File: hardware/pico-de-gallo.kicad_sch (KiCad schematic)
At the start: 7 parts, among them J1 Conn_01x04_Socket, J2 Conn_01x05_Socket, J3 Conn_01x08_Pin

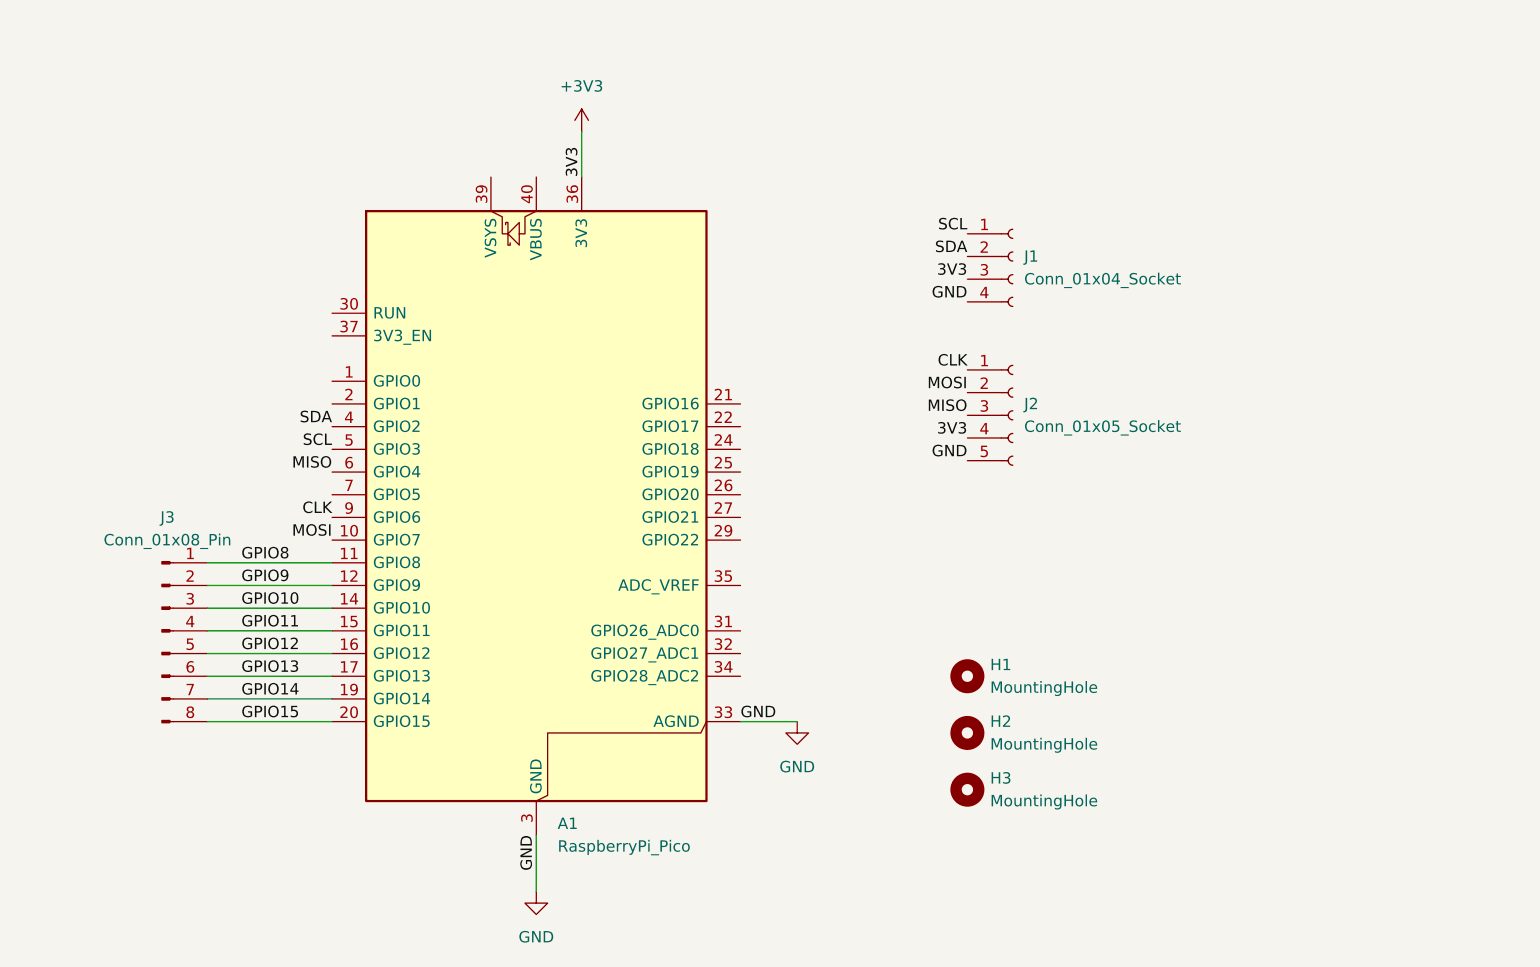
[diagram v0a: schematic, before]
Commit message: hardware: fix DRC and ERC
Signed-off-by: Felipe Balbi <febalbi@microsoft.com>
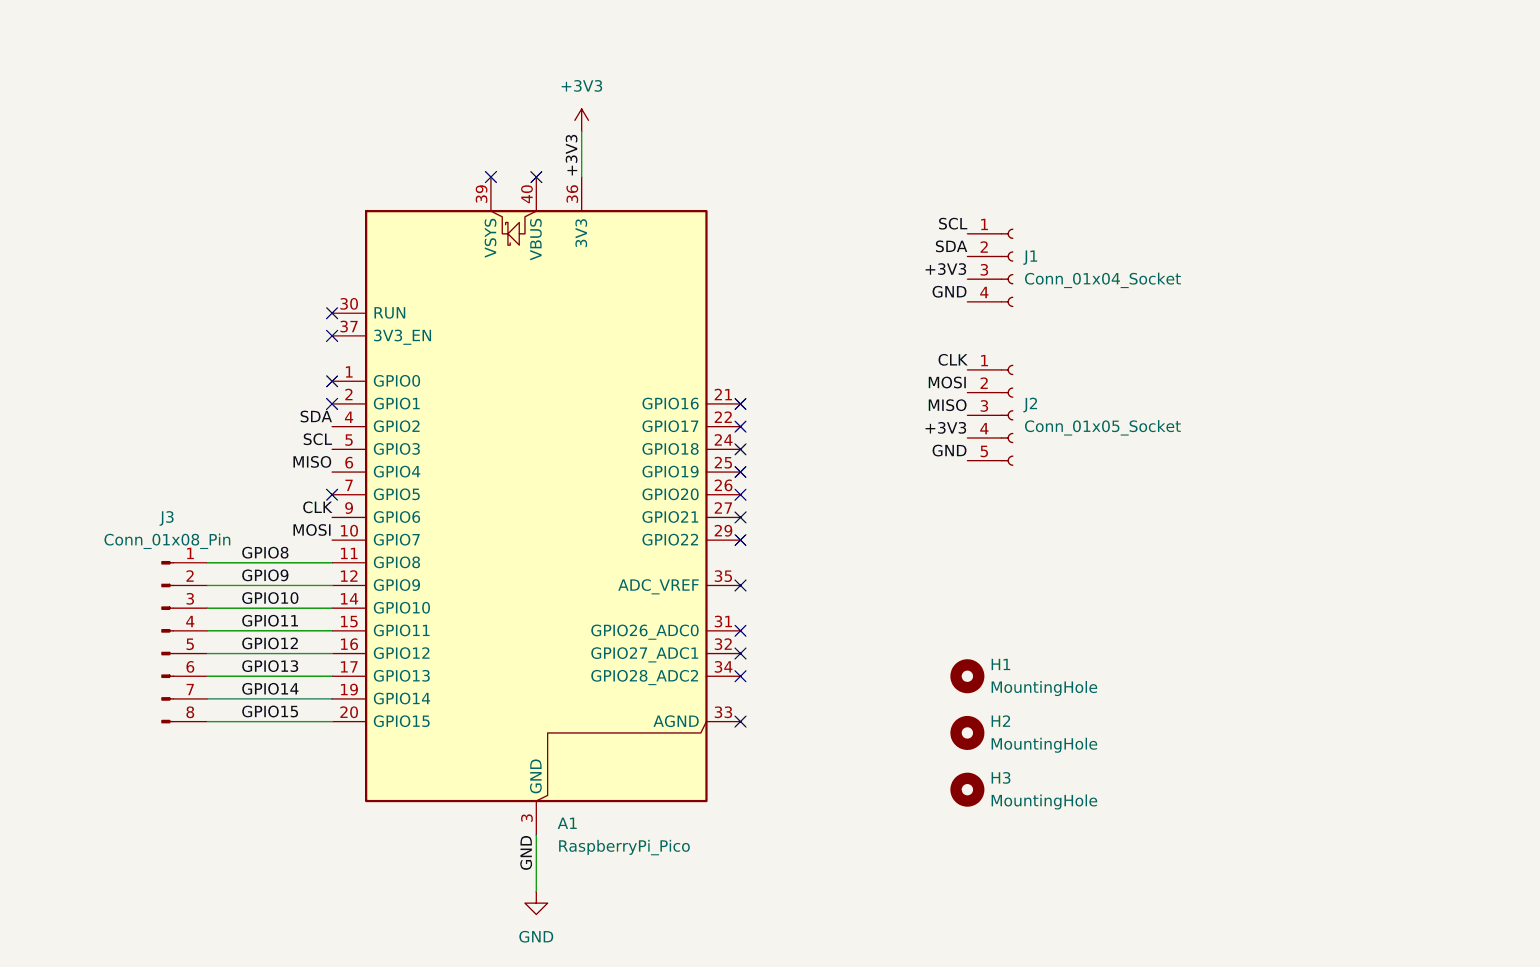
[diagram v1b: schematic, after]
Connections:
- net GND: no longer A1.33 (AGND)
- no-connect marks 0 -> 19
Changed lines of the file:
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@@
 	(generator_version "9.0")
 	(paper "A4")
+	(no_connect
+		(at 146.05 57.15)
+	)
+	(no_connect
+		(at 168.91 87.63)
+	)
+	(no_connect
+		(at 123.19 80.01)
+	)
+	(no_connect
+		(at 123.19 72.39)
+	)
+	(no_connect
+		(at 168.91 82.55)
+	)
+	(no_connect
+		(at 168.91 102.87)
+	)
+	(no_connect
+		(at 168.91 85.09)
+	)
+	(no_connect
+		(at 168.91 90.17)
+	)
+	(no_connect
+		(at 168.91 95.25)
+	)
+	(no_connect
+		(at 168.91 118.11)
+	)
+	(no_connect
+		(at 168.91 92.71)
+	)
+	(no_connect
+		(at 123.19 92.71)
+	)
+	(no_connect
+		(at 123.19 74.93)
+	)
+	(no_connect
+		(at 168.91 110.49)
+	)
+	(no_connect
+		(at 168.91 97.79)
+	)
+	(no_connect
+		(at 140.97 57.15)
+	)
+	(no_connect
+		(at 123.19 82.55)
+	)
+	(no_connect
+		(at 168.91 113.03)
+	)
+	(no_connect
+		(at 168.91 107.95)
+	)
 	(wire
 		(pts
@@
 		(pts
 			(xy 151.13 52.07) (xy 151.13 57.15)
-		)
-		(stroke
-			(width 0)
-			(type default)
-		)
-	)
-	(wire
-		(pts
-			(xy 168.91 118.11) (xy 175.26 118.11)
 		)
 		(stroke
@@
 		)
 	)
-	(label "3V3"
+	(label "+3V3"
 		(at 151.13 57.15 90)
 		(effects
@@
 		)
 	)
-	(label "3V3"
+	(label "+3V3"
 		(at 194.31 68.58 180)
 		(effects
@@
 	)
 	(label "GND"
-		(at 168.91 118.11 0)
-		(effects
-			(font
-				(size 1.27 1.27)
-			)
-			(justify left bottom)
-		)
-	)
-	(label "GND"
 		(at 194.31 88.9 180)
 		(effects
@@
 		)
 	)
-	(label "3V3"
+	(label "+3V3"
 		(at 194.31 86.36 180)
 		(effects
@@
 					(unit 1)
 				)
-			)
-		)
-	)
-	(symbol
-		(lib_id "power:GND")
-		(at 175.26 118.11 0)
-		(unit 1)
-		(exclude_from_sim no)
-		(in_bom yes)
-		(on_board yes)
-		(dnp no)
-		(fields_autoplaced yes)
-		(property "Reference" "#PWR02"
-			(at 175.26 124.46 0)
-			(effects
-				(font
-					(size 1.27 1.27)
-				)
-				(hide yes)
-			)
-		)
-		(property "Value" "GND"
-			(at 175.26 123.19 0)
-			(effects
-				(font
-					(size 1.27 1.27)
-				)
-			)
-		)
-		(property "Footprint" ""
-			(at 175.26 118.11 0)
-			(effects
-				(font
-					(size 1.27 1.27)
-				)
-				(hide yes)
-			)
-		)
-		(property "Datasheet" ""
-			(at 175.26 118.11 0)
-			(effects
-				(font
-					(size 1.27 1.27)
-				)
-				(hide yes)
-			)
-		)
-		(property "Description" "Power symbol creates a global label with name \"GND\" , ground"
-			(at 175.26 118.11 0)
-			(effects
-				(font
-					(size 1.27 1.27)
-				)
-				(hide yes)
-			)
-		)
-		(pin "1"
-		)
-		(instances
-			(project "pico-de-gallo"
-				(path "/409a2a34-92f9-4daa-b11b-cb64dd13f272"
-					(reference "#PWR02")
-					(unit 1)
-				)

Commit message: update case and PCB
Signed-off-by: Felipe Balbi <febalbi@microsoft.com>
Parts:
- removed J1: Conn_01x04_Socket, Connector_PinSocket_2.54mm:PinSocket_1x04_P2.54mm_Horizontal, symbol Connector:Conn_01x04_Socket
- removed J2: Conn_01x05_Socket, Connector_PinSocket_2.54mm:PinSocket_1x05_P2.54mm_Horizontal, symbol Connector:Conn_01x05_Socket
- removed J3: Conn_01x08_Pin, Connector_PinHeader_2.54mm:PinHeader_1x08_P2.54mm_Vertical, symbol Connector:Conn_01x08_Pin
- added J1: Conn_02x08_Odd_Even, Connector_PinHeader_2.54mm:PinHeader_2x08_P2.54mm_Vertical, symbol Connector_Generic:Conn_02x08_Odd_Even
- added J2, J5: Conn_01x02, Connector_PinHeader_2.54mm:PinHeader_1x02_P2.54mm_Vertical, symbol Connector_Generic:Conn_01x02
- added J3: Conn_01x04, Connector_PinHeader_2.54mm:PinHeader_1x04_P2.54mm_Vertical, symbol Connector_Generic:Conn_01x04
- added J4: Conn_01x05, Connector_PinHeader_2.54mm:PinHeader_1x05_P2.54mm_Vertical, symbol Connector_Generic:Conn_01x05
- added J6: Conn_01x03, Connector_PinHeader_2.54mm:PinHeader_1x03_P2.54mm_Vertical, symbol Connector_Generic:Conn_01x03
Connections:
- net +3V3: now also J2.1 (Pin_1), J3.3 (Pin_3), J4.4 (Pin_4)
- net CLK: now also J4.1 (Pin_1), J6.1 (Pin_1)
- net GND: now also J2.2 (Pin_2), J3.4 (Pin_4), J4.5 (Pin_5)
- net GPIO10: now also J1.5 (Pin_5), J1.6 (Pin_6)
- net GPIO11: now also J1.7 (Pin_7), J1.8 (Pin_8)
- net GPIO12: now also J1.10 (Pin_10), J1.9 (Pin_9)
- net GPIO13: now also J1.11 (Pin_11), J1.12 (Pin_12)
- net GPIO14: now also J1.13 (Pin_13), J1.14 (Pin_14)
- net GPIO15: now also J1.15 (Pin_15), J1.16 (Pin_16)
- net GPIO8: now also J1.1 (Pin_1), J1.2 (Pin_2)
- net GPIO9: now also J1.3 (Pin_3), J1.4 (Pin_4)
- net MISO: now also J4.3 (Pin_3), J6.3 (Pin_3)
- net MOSI: now also J4.2 (Pin_2), J6.2 (Pin_2)
- net SCL: now also J3.1 (Pin_1), J5.1 (Pin_1)
- net SDA: now also J3.2 (Pin_2), J5.2 (Pin_2)

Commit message: Update PCB
Signed-off-by: Felipe Balbi <febalbi@microsoft.com>
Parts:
- J3: footprint Connector_PinHeader_2.54mm:PinHeader_1x04_P2.54mm_Vertical -> Connector_PinSocket_2.54mm:PinSocket_1x04_P2.54mm_Horizontal
- J4: footprint Connector_PinHeader_2.54mm:PinHeader_1x05_P2.54mm_Vertical -> Connector_PinSocket_2.54mm:PinSocket_1x05_P2.54mm_Horizontal
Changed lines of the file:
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@@
 			)
 		)
-		(property "Footprint" "Connector_PinHeader_2.54mm:PinHeader_1x04_P2.54mm_Vertical"
+		(property "Footprint" "Connector_PinSocket_2.54mm:PinSocket_1x04_P2.54mm_Horizontal"
 			(at 199.39 66.04 0)
 			(effects
@@
 			)
 		)
-		(property "Footprint" "Connector_PinHeader_2.54mm:PinHeader_1x05_P2.54mm_Vertical"
+		(property "Footprint" "Connector_PinSocket_2.54mm:PinSocket_1x05_P2.54mm_Horizontal"
 			(at 199.39 83.82 0)
 			(effects

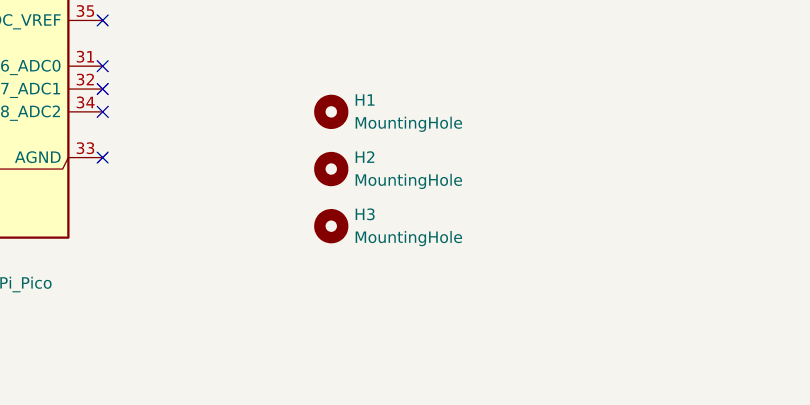
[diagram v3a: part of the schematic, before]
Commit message: Update schematics and PCB
Right angle headers

Signed-off-by: Felipe Balbi <febalbi@microsoft.com>
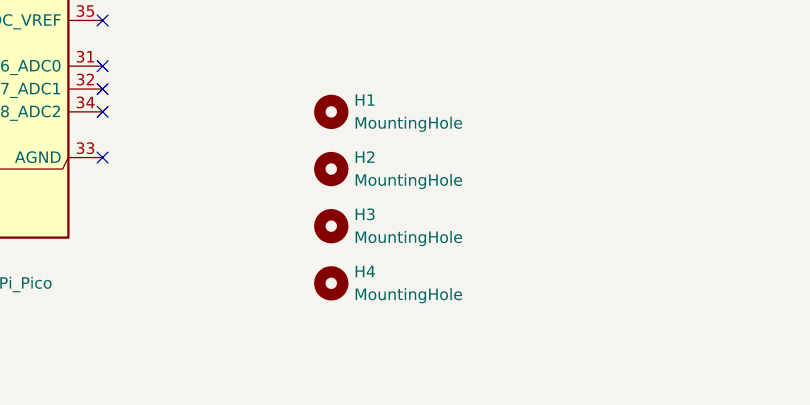
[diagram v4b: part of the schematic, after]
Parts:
- added H4: MountingHole, MountingHole:MountingHole_3.2mm_M3, symbol Mechanical:MountingHole
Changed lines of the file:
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@@
+	)
+	(symbol
+		(lib_id "Mechanical:MountingHole")
+		(at 194.31 132.08 0)
+		(unit 1)
+		(exclude_from_sim no)
+		(in_bom no)
+		(on_board yes)
+		(dnp no)
+		(fields_autoplaced yes)
+		(property "Reference" "H4"
+			(at 196.85 130.8099 0)
+			(effects
+				(font
+					(size 1.27 1.27)
+				)
+				(justify left)
+			)
+		)
+		(property "Value" "MountingHole"
+			(at 196.85 133.3499 0)
+			(effects
+				(font
+					(size 1.27 1.27)
+				)
+				(justify left)
+			)
+		)
+		(property "Footprint" "MountingHole:MountingHole_3.2mm_M3"
+			(at 194.31 132.08 0)
+			(effects
+				(font
+					(size 1.27 1.27)
+				)
+				(hide yes)
+			)
+		)
+		(property "Datasheet" "~"
+			(at 194.31 132.08 0)
+			(effects
+				(font
+					(size 1.27 1.27)
+				)
+				(hide yes)
+			)
+		)
+		(property "Description" "Mounting Hole without connection"
+			(at 194.31 132.08 0)
+			(effects
+				(font
+					(size 1.27 1.27)
+				)
+				(hide yes)
+			)
+		)
+		(instances
+			(project "pico-de-gallo"
+				(path "/409a2a34-92f9-4daa-b11b-cb64dd13f272"
+					(reference "H4")
+					(unit 1)
+				)
+			)
+		)
 	)
 	(symbol

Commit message: hardware: include totalphase beagle analyzer footprint
useful for debugging.

Signed-off-by: Felipe Balbi <febalbi@microsoft.com>
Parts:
- added J7: Conn_02x05_Odd_Even, Connector_PinHeader_2.54mm:PinHeader_2x05_P2.54mm_Vertical_SMD, symbol Connector_Generic:Conn_02x05_Odd_Even
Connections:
- net CLK: now also J7.7 (Pin_7)
- net GND: now also J7.10 (Pin_10), J7.2 (Pin_2)
- net MISO: now also J7.5 (Pin_5)
- net MOSI: now also J7.8 (Pin_8)
- net SCL: now also J7.1 (Pin_1)
- net SDA: now also J7.3 (Pin_3)
- net GPIO10 renamed GPIO2
- net GPIO11 renamed GPIO3
- net GPIO12 renamed GPIO4
- net GPIO13 renamed GPIO5
- net GPIO14 renamed GPIO6
- net GPIO15 renamed GPIO7
- net GPIO8 renamed GPIO0
- net GPIO0: now also J7.9 (Pin_9)
- net GPIO9 renamed GPIO1
- no-connect marks 19 -> 21
